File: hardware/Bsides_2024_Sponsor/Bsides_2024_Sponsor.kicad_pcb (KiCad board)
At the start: 2 copper layers, 139.6 x 137 mm, 45 parts, among them J1 Conn_02x03_Odd_Even, J2 Battery, J3 Battery, J4 OLED, P1 USB_C_Plug_USB2.0, Q1 DMG3415U-7, SW1 ON, SW2 RESET, SW3 BOOT, SW4 RESET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

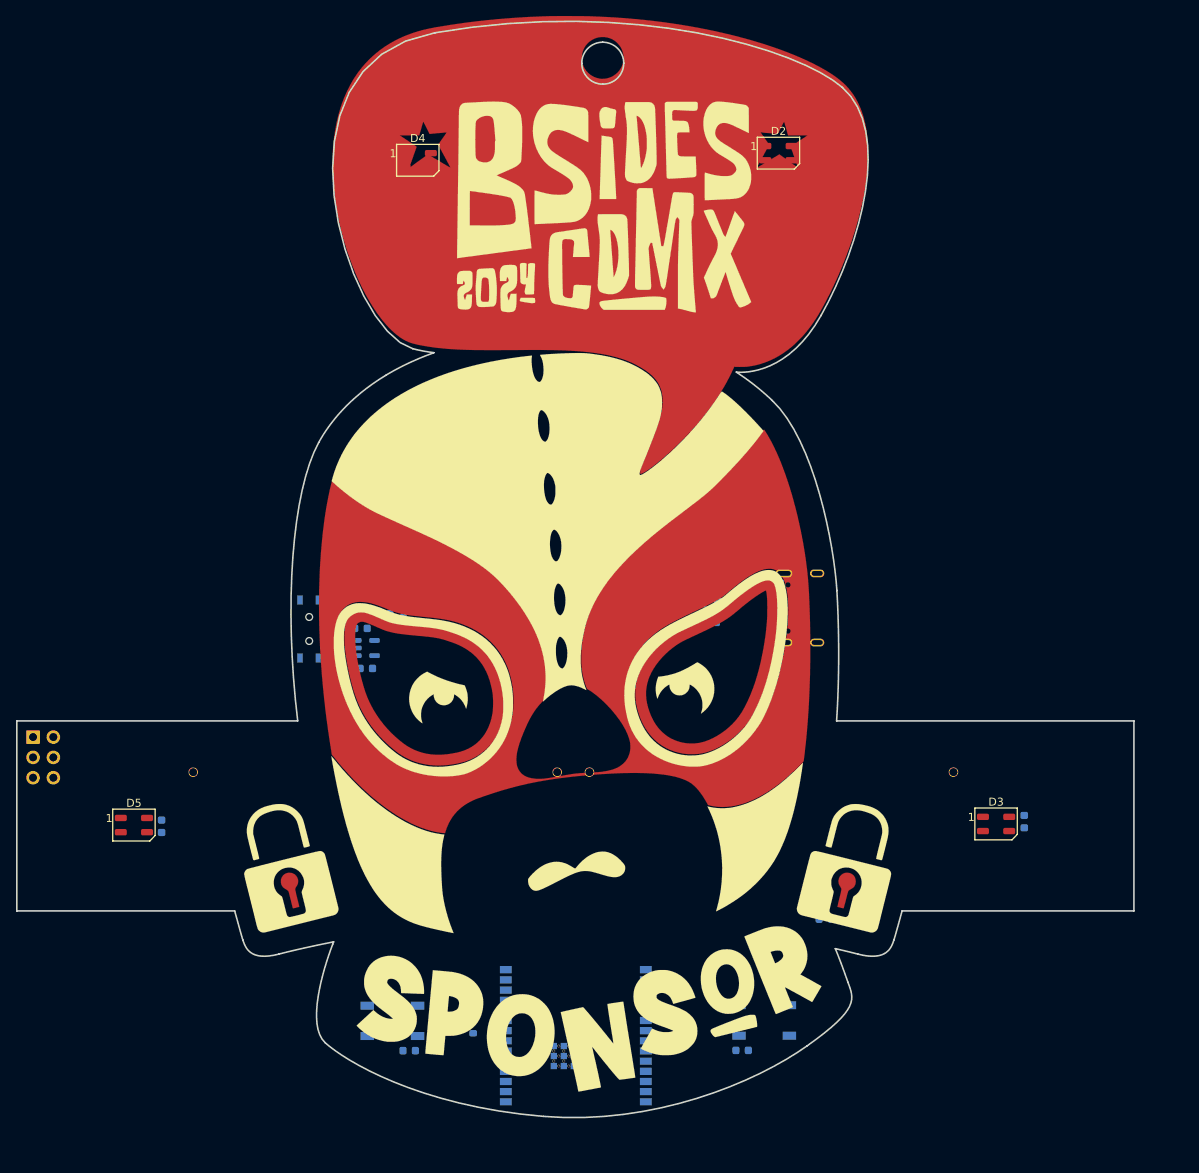
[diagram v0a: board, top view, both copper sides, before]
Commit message: feat(Hw):Added_speaker_Badge_Floorplan
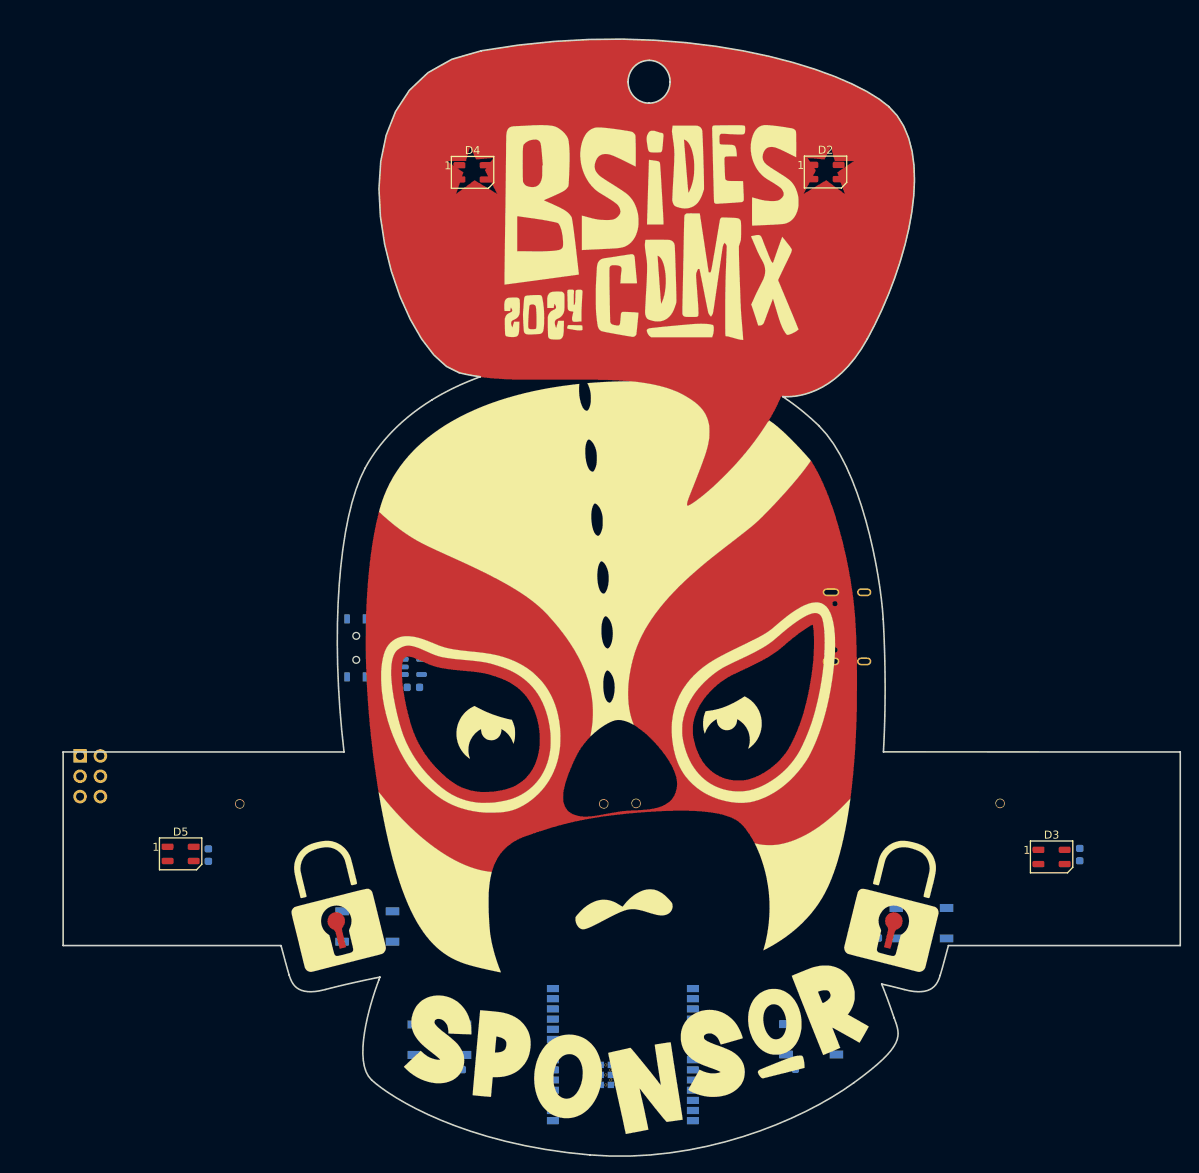
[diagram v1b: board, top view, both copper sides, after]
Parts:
- removed the Ref** at (135.6, 80.0) (x2)
- removed the Ref** at (135.3, 115.9) (x2)
- removed the Ref** at (137.0, 75.6)
- removed the Ref** at (136.2, 92.4)
- added Ref**: Val**, Sponsor:Badge Sponsor_Bsides 2024 CDMX (1), F.Cu at (128.3, 76.2)
- moved SW5 10.7 mm to (111.1, 133.6)
- moved SW4 10.2 mm to (180.4, 133.2)
- moved C6 8.07 mm to (200.2, 124.7)
- moved D3 8.07 mm to (196.7, 124.9)
- moved J4 7.90 mm to (125.9, 79.5)
- moved J2 7.04 mm to (118.0, 118.3)
- moved J3 7.02 mm to (167.5, 118.2)
- moved D4 7.01 mm to (124.3, 39.4)
- moved D5 6.86 mm to (87.8, 124.6)
- moved C12 6.86 mm to (91.3, 124.7)
- moved C3 6.34 mm to (170.4, 53.7)
- moved C8 6.34 mm to (174.3, 135.1)
- moved C11 6.34 mm to (122.3, 151.5)
- moved C2 6.34 mm to (116.9, 103.7)
- moved D1 6.34 mm to (117.0, 96.7)
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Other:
- board size 139.6 x 137 mm -> 139.6 x 139.6 mm

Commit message: feat(Hw):Update_Floorplan_Sponsor
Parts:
- removed J1: Conn_02x03_Odd_Even, Connector_PinSocket_2.54mm:PinSocket_2x03_P2.54mm_Vertical
- added C13: 1uF, Capacitor_SMD:C_0603_1608Metric, B.Cu at (128.6, 157.1)
- added C14: 10uF, Capacitor_SMD:C_0603_1608Metric, B.Cu at (130.1, 157.1)
- added C15: 10uF, Capacitor_SMD:C_0603_1608Metric, B.Cu at (131.6, 157.1)
- added J5: Add_On, Connector_PinSocket_2.54mm:PinSocket_2x03_P2.54mm_Vertical, F.Cu at (120.9, 69.4)
- J4: moved to F.Cu
- moved J4 49.0 mm to (90.8, 113.7), turned to -90 degrees
- moved J3 23.7 mm to (147.6, 105.4), turned to -90 degrees
- moved J2 20.2 mm to (133.4, 105.3), turned to 90 degrees
- moved C1 9.64 mm to (125.7, 100.4), turned to -90 degrees
- moved U2 6.13 mm to (122.9, 100.6), turned to 180 degrees
- moved Q1 5.04 mm to (116.1, 98.7), turned to 90 degrees
- moved C2 3.68 mm to (118.6, 100.5), turned to -90 degrees
- moved R2 3.67 mm to (120.1, 100.4), turned to -90 degrees
- moved D1 1.33 mm to (116.3, 95.5)
- moved SW1 1.06 mm to (109.6, 97.8)
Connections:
- C1 pad 1: Net-(SW1-B) -> VBUS
- C12 pad 2: +3V3 -> /VOUT
- C2 pad 1: +3V3 -> Net-(D1-A)
- C5 pad 2: +3V3 -> /VOUT
- C6 pad 2: +3V3 -> /VOUT
- C7 pad 2: +3V3 -> /VOUT
- D1 pad 2: VBUS -> Net-(D1-A)
- D2 pad 1: +3V3 -> /VOUT
- D3 pad 1: +3V3 -> /VOUT
- D4 pad 1: +3V3 -> /VOUT
- D5 pad 1: +3V3 -> /VOUT
- Q1 pad 1: VBUS -> Net-(D1-A)
- R1 pad 2: +3V3 -> /VOUT
- R2 pad 1: VBUS -> Net-(D1-A)
- R5 pad 2: +3V3 -> /VOUT
- SW1 pad 2: Net-(SW1-B) -> /VOUT
- U1 pad 2: +3V3 -> /VOUT
- U2 pad 1: Net-(SW1-B) -> VBUS
- U2 pad 3: Net-(SW1-B) -> VBUS
- U2 pad 5: +3V3 -> Net-(D1-A)

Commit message: feat:(Hw)Update_PCB_Speaker_Sponsor_Staff
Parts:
- removed the Ref** at (128.3, 76.2)
- added Ref**: Val**, Sponsor:Badge_Sponsor_Bsides_2024_CDMX, F.Cu at (128.4, 76.2)
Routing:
- added copper zone on F.Cu, net GND

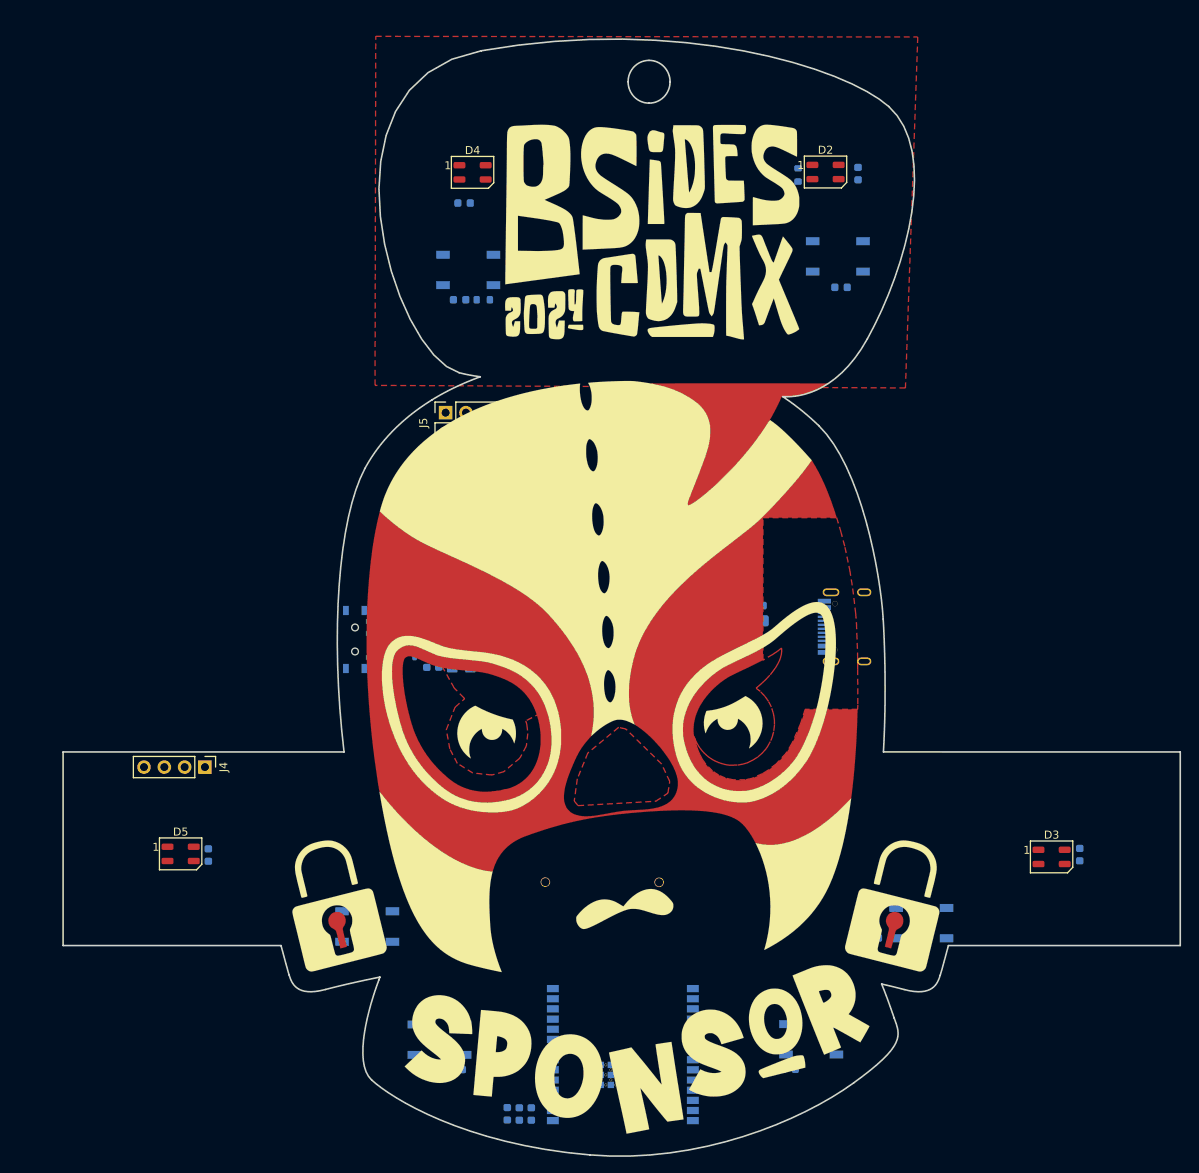
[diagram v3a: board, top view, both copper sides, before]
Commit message: feat(Hw):update_floorplan_sponsor
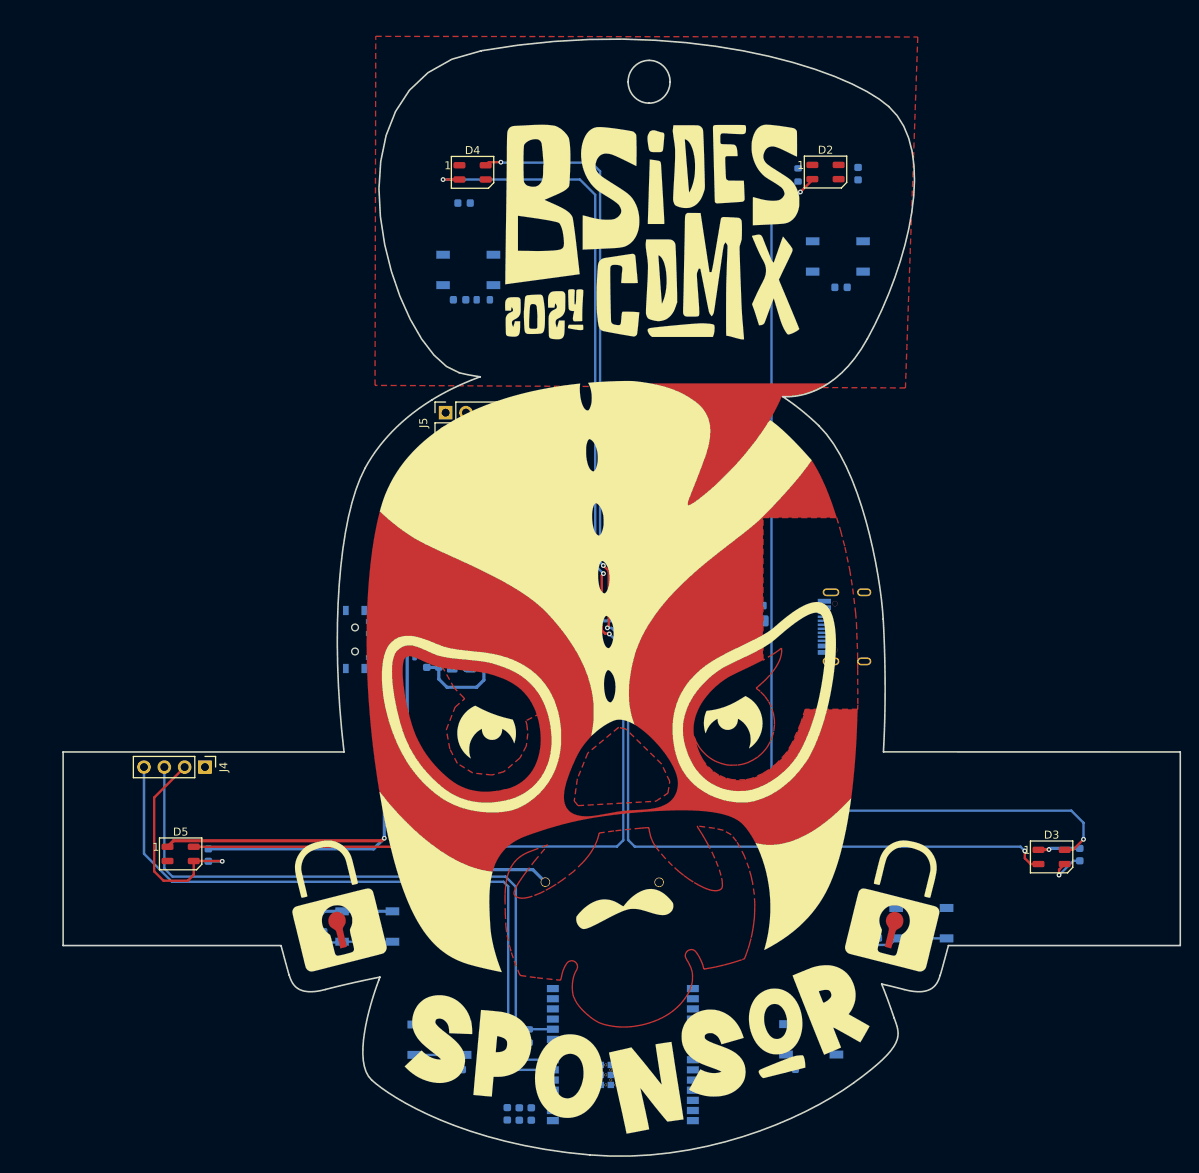
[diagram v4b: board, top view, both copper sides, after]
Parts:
- moved R1 1.64 mm to (131.4, 147.3)
- moved C9 1.36 mm to (104.9, 134.3)
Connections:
- J4 pad 1: +3V3 -> /VOUT
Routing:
- net Net-(D4-DOUT): track 0.00 -> 158.5 mm, vias 0 -> 4
- net Net-(D3-DOUT): track 0.00 -> 153.5 mm, vias 0 -> 4
- net Net-(D2-DOUT): track 0.00 -> 124.8 mm, vias 0 -> 2
- net /SDA: track 0.00 -> 85.8 mm
- net /SCL: track 0.00 -> 83.6 mm
- net /VOUT: track 0.00 -> 82.4 mm, vias 0 -> 2
- net GND: track 0.00 -> 56.8 mm, vias 0 -> 2
- net +BATT: track 0.00 -> 46.0 mm
- net VBUS: track 0.00 -> 42.3 mm
- net /GPIO1: track 0.00 -> 10.8 mm
- net /GPIO22: track 0.00 -> 10.7 mm
- net Net-(D1-A): track 0.00 -> 9.15 mm
- net /GPIO23: track 0.00 -> 8.24 mm
- net Net-(D1-K): track 0.00 -> 7.60 mm
- net /PIN: track 0.00 -> 2.97 mm

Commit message: feat(Hw):Update_Route_Sponsor
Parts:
- added J1: Serial_IN, Connector_PinSocket_2.54mm:PinSocket_1x03_P2.54mm_Vertical, F.Cu at (211.0, 126.4)
- added J6: Battery, bsides:BH-AA-A1AJ020, B.Cu at (135.3, 56.8)
- C1: value 10uF -> 1uF
- C10, C9, R6: moved to F.Cu
- C13: value 1uF -> 0.1uF
- C14: value 10uF -> 0.1uF
- C15: value 10uF -> 0.1uF; moved to F.Cu
- C3, C4, C5: value 0.1uF -> 10uF
- J2: value Battery -> Add_On; footprint bsides:BH-AAA-A1aj001 -> Connector_PinSocket_2.54mm:PinSocket_2x03_P2.54mm_Vertical; moved to F.Cu
- J3: value Battery -> OLED; footprint bsides:BH-AAA-A1aj001 -> bsides:Display OLED 128 x32; moved to F.Cu
- J4: value OLED -> Serial_OUT; footprint bsides:Display OLED 128 x32 -> Connector_PinHeader_2.54mm:PinHeader_1x03_P2.54mm_Vertical; moved to B.Cu
- J5: value Add_On -> Battery; footprint Connector_PinSocket_2.54mm:PinSocket_2x03_P2.54mm_Vertical -> bsides:BH-AA-A1AJ020; moved to B.Cu
- U1: value ESP32-C6-WROOM-1U-N4 -> ESP32-C6-WROOM-1-N4
- moved D2 117.3 mm to (88.0, 124.8), turned to 180 degrees
- moved R6 116.1 mm to (89.0, 127.5), turned to 180 degrees
- moved C3 112.9 mm to (130.0, 159.2)
- moved C10 112.5 mm to (173.1, 39.3), turned to -90 degrees
- moved D3 112.2 mm to (124.4, 39.1), turned to 180 degrees
- moved D5 108.7 mm to (196.5, 124.4)
- moved C9 96.5 mm to (128.5, 40.7), turned to 90 degrees
- moved C8 89.8 mm to (85.6, 120.8), turned to 0 degrees
- moved C4 87.7 mm to (181.1, 120.7), turned to 90 degrees
- moved C6 86.5 mm to (123.2, 85.3), turned to -90 degrees
- moved C5 84.1 mm to (183.4, 122.9), turned to 180 degrees
- moved SW1 81.6 mm to (189.5, 114.3), turned to 0 degrees
- moved C12 79.8 mm to (171.1, 123.6), turned to -90 degrees
- moved D1 78.9 mm to (191.0, 121.0), turned to -90 degrees
- moved Q1 75.0 mm to (187.9, 120.5), turned to 0 degrees
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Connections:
- C1 pad 1: VBUS -> /VOUT
- C10 pad 2: /GPIO15 -> /VOUT
- C11 pad 2: /GPIO23 -> /GPIO1
- C12 pad 2: /VOUT -> /GPIO15
- C13 pad 1: /VOUT -> GND
- C13 pad 2: GND -> /GPIO22
- C14 pad 1: /VOUT -> GND
- C14 pad 2: GND -> /GPIO23
- C15 pad 1: /VOUT -> GND
- C15 pad 2: GND -> /VOUT
- C2 pad 1: Net-(D1-A) -> /VOUT
- C3 pad 1: GND -> /VOUT
- C3 pad 2: /BOOT -> GND
- C4 pad 1: GND -> VBUS
- C4 pad 2: /EN -> GND
- C5 pad 1: GND -> Net-(D1-A)
- C5 pad 2: /VOUT -> GND
- C6 pad 2: /VOUT -> /BOOT
- C7 pad 2: /VOUT -> /EN
- C8 pad 2: /GPIO1 -> /VOUT
- C9 pad 2: /GPIO22 -> /VOUT
- J2 pad 1: Net-(J2-Pin_1) -> /VOUT
- J2 pad 2: +BATT -> GND
- J3 pad 1: GND -> /SDA
- J3 pad 2: Net-(J2-Pin_1) -> /SCL
- J4 pad 1: /VOUT -> /GPIO4
- J4 pad 2: GND -> /GPIO5
- J4 pad 3: /SCL -> GND
- J5 pad 1: /VOUT -> Net-(J5-Pin_1)
- J5 pad 2: GND -> +BATT
- R1 pad 1: /PIN -> Net-(U1-IO8)
- SW1 pad 2: /VOUT -> Net-(D1-K)
- SW1 pad 3: Net-(D1-K) -> /VOUT
- SW5 pad 2: /GPIO22 -> /GPIO15
- SW6 pad 2: /GPIO15 -> /GPIO22
- U1 pad 10: /PIN -> Net-(U1-IO8)
- U1 pad 11: unconnected-(U1-IO10-Pad11) -> /PIN
- U1 pad 24: /RX -> /GPIO17
- U1 pad 25: /TX -> /GPIO16
- U1 pad 26: unconnected-(U1-IO3-Pad26) -> /GPIO3
- U1 pad 27: unconnected-(U1-IO2-Pad27) -> /GPIO2
- U1 pad 4: unconnected-(U1-IO4-Pad4) -> /GPIO4
- U1 pad 5: unconnected-(U1-IO5-Pad5) -> /GPIO5
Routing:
- net /VOUT: track 82.4 -> 402.0 mm, vias 2 -> 7
- net /GPIO3: track 0.00 -> 115.6 mm, vias 0 -> 1
- net /GPIO2: track 0.00 -> 114.4 mm, vias 0 -> 1
- net Net-(D3-DOUT): track 153.5 -> 42.1 mm, vias 4 -> 0
- net /BOOT: track 0.00 -> 95.5 mm, vias 0 -> 2
- net GND: track 56.8 -> 146.8 mm, vias 2 -> 10
- net /PIN: track 2.97 -> 90.1 mm, vias 0 -> 1
- net /D-: track 0.00 -> 86.6 mm
- net /GPIO5: track 0.00 -> 84.7 mm
- net /GPIO4: track 0.00 -> 84.5 mm
- net /D+: track 0.00 -> 84.2 mm
- net /GPIO17: track 0.00 -> 83.4 mm
- net /GPIO16: track 0.00 -> 82.5 mm
- net /EN: track 0.00 -> 80.9 mm, vias 0 -> 2
- net /GPIO15: track 0.00 -> 53.4 mm
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- added copper zone on B.Cu, net GND
